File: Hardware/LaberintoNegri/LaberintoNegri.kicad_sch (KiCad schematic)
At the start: 42 parts

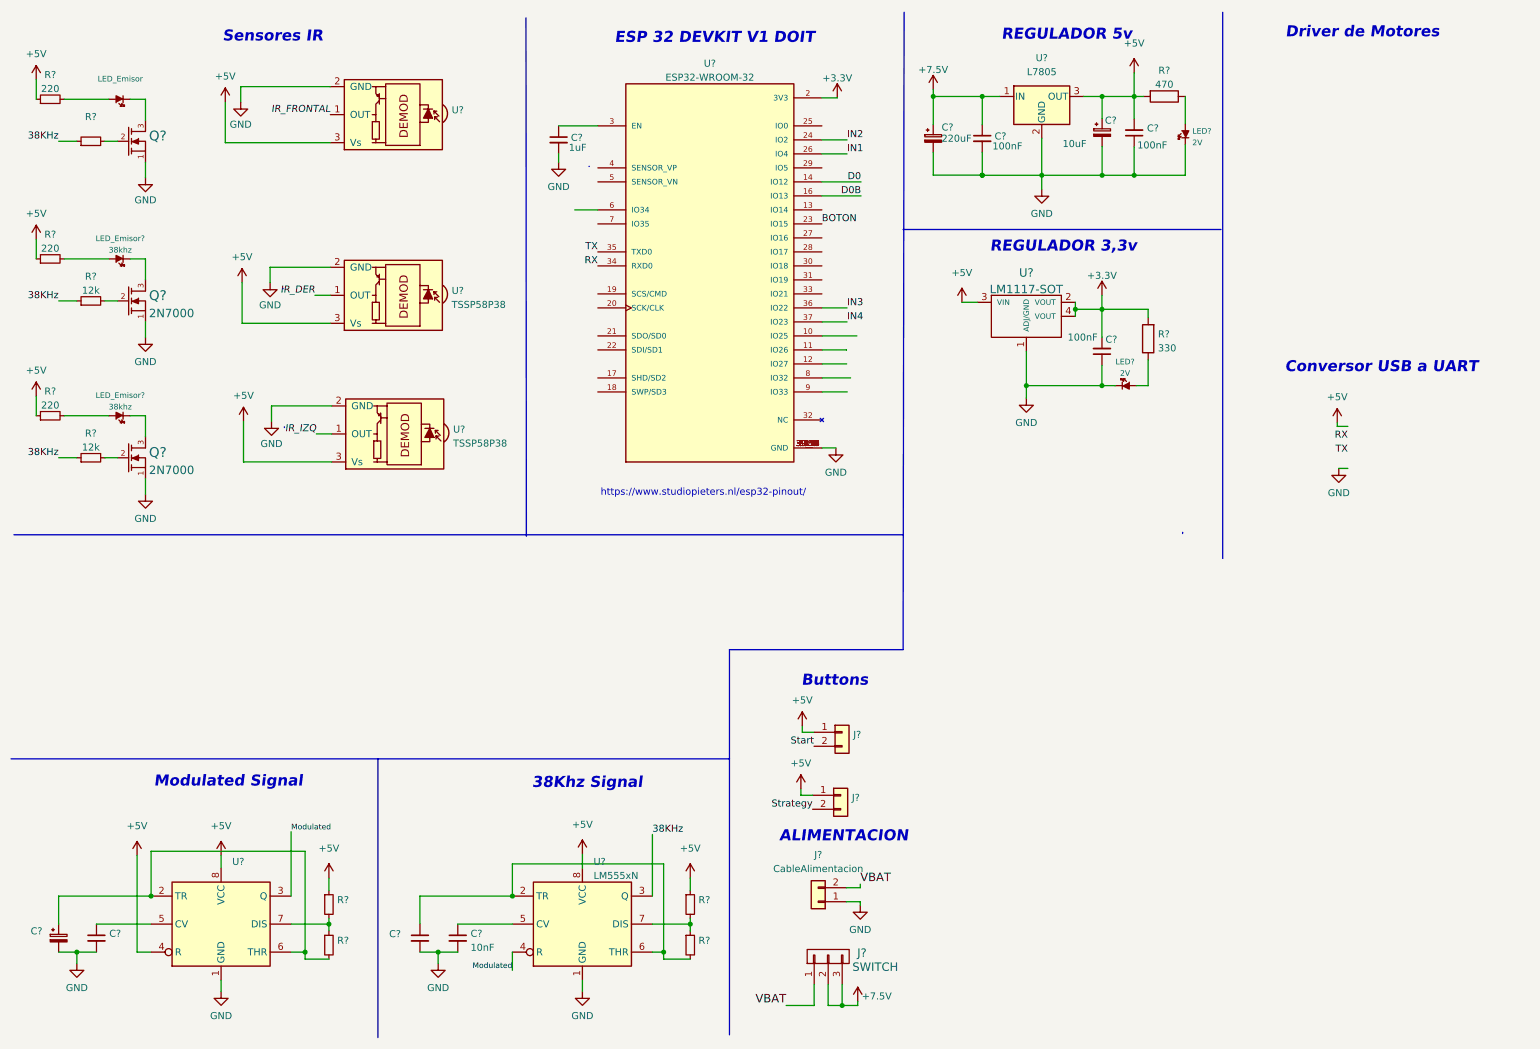
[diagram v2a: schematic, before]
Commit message: subo el sch con el esp32 ya listo como para programar, faltan conexiones y definir el driver
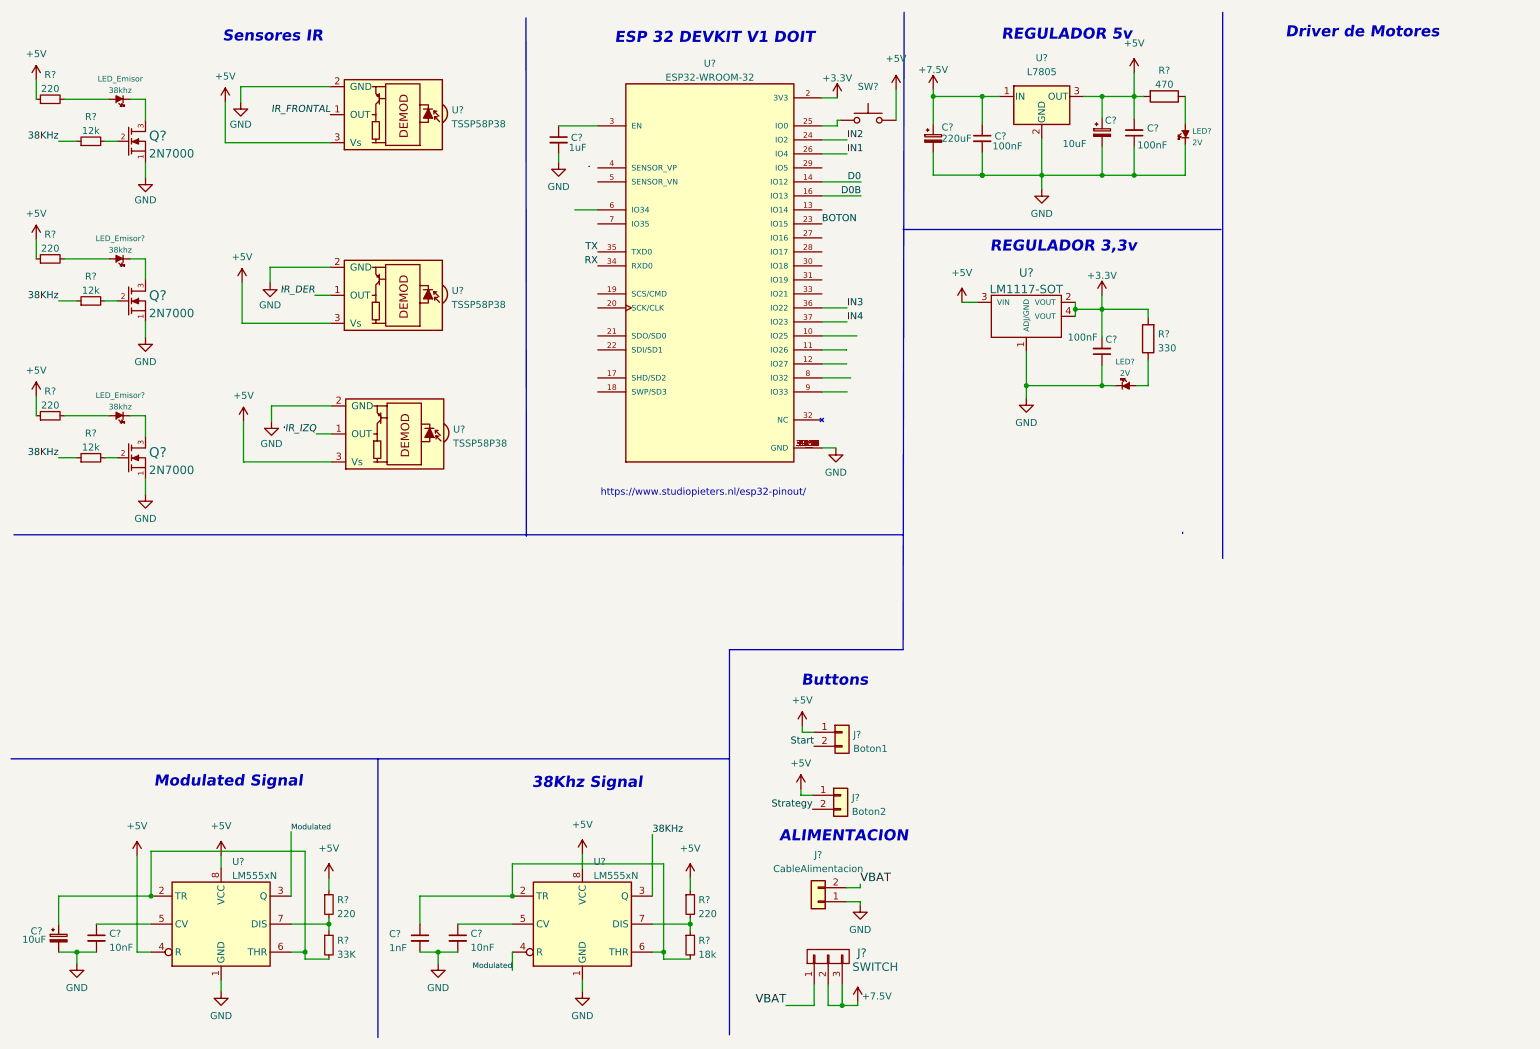
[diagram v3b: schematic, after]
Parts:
- added SW?: SW_Push, symbol EESTN5:SW_Push
- C?: value (none) -> 10uF
- C?: value (none) -> 10nF
- C?: value (none) -> 1nF
- J?: value (none) -> Boton2
- J?: value (none) -> Boton1
- LED_Emisor: value (none) -> 38khz
- Q?: value (none) -> 2N7000; footprint (none) -> EESTN5:SOT23
- R? (x2): value (none) -> 220
- R?: value (none) -> 18k
- R?: value (none) -> 33K
- R?: value (none) -> 12k
- U?: value (none) -> TSSP58P38; footprint (none) -> OptoDevice:Vishay_MINICAST-3Pin
- U?: value (none) -> LM555xN; footprint (none) -> Package_DIP:DIP-8_W7.62mm
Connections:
- net +5V: now also SW?.2
- net at U?.25 (IO0): now also SW?.1
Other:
- note removed: "Conversor USB a UART"
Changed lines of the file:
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@@
     (stroke (width 0) (type default) (color 0 0 0 0))
   )
+  (wire (pts (xy 161.544 32.512) (xy 161.544 31.496))
+    (stroke (width 0) (type default) (color 0 0 0 0))
+  )
   (wire (pts (xy 27.178 177.292) (xy 37.084 177.292))
     (stroke (width 0) (type default) (color 0 0 0 0))
@@
     (stroke (width 0) (type default) (color 0 0 0 0))
   )
+  (wire (pts (xy 161.544 31.496) (xy 162.052 31.496))
+    (stroke (width 0) (type default) (color 0 0 0 0))
+  )
   (wire (pts (xy 65.024 164.084) (xy 37.084 164.084))
     (stroke (width 0) (type default) (color 0 0 0 0))
@@
     (stroke (width 0) (type default) (color 0 0 0 0))
   )
+  (wire (pts (xy 158.75 32.512) (xy 161.544 32.512))
+    (stroke (width 0) (type default) (color 0 0 0 0))
+  )
   (wire (pts (xy 209.55 79.629) (xy 195.834 79.629))
     (stroke (width 0) (type default) (color 0 0 0 0))
@@
     (stroke (width 0) (type default) (color 0 0 0 0))
   )
-  (wire (pts (xy 252.5014 94.6404) (xy 254.1524 94.6404))
-    (stroke (width 0) (type default) (color 0 0 0 0))
-  )
   (wire (pts (xy 28.702 92.71) (xy 30.988 92.71))
     (stroke (width 0) (type default) (color 0 0 0 0))
@@
     (stroke (width 0) (type default) (color 0 0 0 0))
   )
+  (wire (pts (xy 172.212 25.908) (xy 172.212 31.496))
+    (stroke (width 0) (type default) (color 0 0 0 0))
+  )
   (wire (pts (xy 158.75 70.612) (xy 165.1 70.612))
     (stroke (width 0) (type default) (color 0 0 0 0))
@@
     (stroke (width 0) (type default) (color 0 0 0 0))
   )
-  (wire (pts (xy 252.222 87.0204) (xy 252.222 86.36))
-    (stroke (width 0) (type default) (color 0 0 0 0))
-  )
-  (wire (pts (xy 254.1524 87.0204) (xy 252.222 87.0204))
-    (stroke (width 0) (type default) (color 0 0 0 0))
-  )
   (wire (pts (xy 16.256 81.534) (xy 16.256 85.09))
     (stroke (width 0) (type default) (color 0 0 0 0))
@@
     (effects (font (size 2 2) (thickness 0.4) bold italic) (justify left bottom))
   )
-  (text "Conversor USB a UART" (at 242.7224 77.4954 0)
-    (effects (font (size 2 2) (thickness 0.4) bold italic) (justify left bottom))
-  )
   (text "ALIMENTACION\n" (at 151.003 162.5854 0)
     (effects (font (size 2 2) (thickness 0.254) bold italic) (justify left bottom))
@@
     (effects (font (size 1.524 1.524)) (justify right bottom))
   )
-  (label "RX" (at 254.1524 89.5604 180)
-    (effects (font (size 1.27 1.27)) (justify right bottom))
-  )
   (label "IN3" (at 163.322 65.532 0)
     (effects (font (size 1.27 1.27)) (justify left bottom))
@@
     (effects (font (size 1.27 1.27)) (justify left bottom))
   )
-  (label "TX" (at 254.1524 92.1004 180)
-    (effects (font (size 1.27 1.27)) (justify right bottom))
-  )
   (label "D0B" (at 165.862 45.212 180)
     (effects (font (size 1.27 1.27)) (justify right bottom))
@@
       (effects (font (size 1.27 1.27)) (justify left))
     )
-    (property "Value" "" (id 1) (at 13.716 180.086 0)
+    (property "Value" "10uF" (id 1) (at 13.716 180.086 0)
       (effects (font (size 1.27 1.27)) (justify left))
     )
@@
       (effects (font (size 1.27 1.27)) (justify left))
     )
-    (property "Value" "" (id 1) (at 136.3726 175.4382 0)
+    (property "Value" "220" (id 1) (at 136.3726 175.4382 0)
       (effects (font (size 1.27 1.27)) (justify left))
     )
@@
       (effects (font (size 1.27 1.27)) (justify left))
     )
-    (property "Value" "" (id 1) (at 164.1856 156.8962 0)
+    (property "Value" "Boton2" (id 1) (at 164.1856 156.8962 0)
       (effects (font (size 1.27 1.27)) (justify left))
     )
@@
       (effects (font (size 1.016 1.016)))
     )
-    (property "Value" "" (id 1) (at 31.496 26.07 0)
+    (property "Value" "38khz" (id 1) (at 31.496 26.07 0)
       (effects (font (size 1.016 1.016)))
     )
@@
     (pin "7")
   )
-  (symbol (lib_id "power:GND") (at 252.5014 94.6404 0) (unit 1)
-    (in_bom yes) (on_board yes) (fields_autoplaced)
-    (property "Reference" "#PWR?" (id 0) (at 252.5014 100.9904 0)
-      (effects (font (size 1.27 1.27)) hide)
-    )
-    (property "Value" "GND" (id 1) (at 252.5014 99.0838 0))
-    (property "Footprint" "" (id 2) (at 252.5014 94.6404 0)
-      (effects (font (size 1.27 1.27)) hide)
-    )
-    (property "Datasheet" "" (id 3) (at 252.5014 94.6404 0)
-      (effects (font (size 1.27 1.27)) hide)
-    )
-    (pin "1")
-  )
   (symbol (lib_id "power:GND") (at 161.29 90.932 0) (unit 1)
     (in_bom yes) (on_board yes) (fields_autoplaced)
@@
       (effects (font (size 1.27 1.27)) (justify left))
     )
-    (property "Value" "" (id 1) (at 136.3726 182.8042 0)
+    (property "Value" "18k" (id 1) (at 136.3726 182.8042 0)
       (effects (font (size 1.27 1.27)) (justify left))
     )
@@
       (effects (font (size 1.778 1.778)) (justify left))
     )
-    (property "Value" "" (id 1) (at 36.703 37.5515 0)
+    (property "Value" "2N7000" (id 1) (at 36.703 37.5515 0)
       (effects (font (size 1.524 1.524)) (justify left))
     )
-    (property "Footprint" "" (id 2) (at 33.528 35.306 0)
+    (property "Footprint" "EESTN5:SOT23" (id 2) (at 33.528 35.306 0)
       (effects (font (size 1.524 1.524)) hide)
     )
@@
       (effects (font (size 1.27 1.27)) (justify left))
     )
-    (property "Value" "" (id 1) (at 70.8406 175.4382 0)
+    (property "Value" "220" (id 1) (at 70.8406 175.4382 0)
       (effects (font (size 1.27 1.27)) (justify left))
     )
@@
       (effects (font (size 1.27 1.27)) (justify left))
     )
-    (property "Value" "" (id 1) (at 70.8406 182.8042 0)
+    (property "Value" "33K" (id 1) (at 70.8406 182.8042 0)
       (effects (font (size 1.27 1.27)) (justify left))
     )
@@
     (in_bom yes) (on_board yes) (fields_autoplaced)
     (property "Reference" "R?" (id 0) (at 26.162 30.8696 90))
-    (property "Value" "" (id 1) (at 26.162 33.4065 90))
+    (property "Value" "12k" (id 1) (at 26.162 33.4065 90))
     (property "Footprint" "" (id 2) (at 26.162 35.306 0)
       (effects (font (size 1.27 1.27)) hide)
@@
       (effects (font (size 1.27 1.27)) (justify left))
     )
-    (property "Value" "" (id 1) (at 29.5021 181.5405 0)
+    (property "Value" "10nF" (id 1) (at 29.5021 181.5405 0)
       (effects (font (size 1.27 1.27)) (justify left))
     )
@@
     (pin "1")
   )
+  (symbol (lib_id "EESTN5:SW_Push") (at 167.132 31.496 0) (unit 1)
+    (in_bom yes) (on_board yes) (fields_autoplaced)
+    (property "Reference" "SW?" (id 0) (at 167.132 25.4 0))
+    (property "Value" "SW_Push" (id 1) (at 167.132 33.02 0)
+      (effects (font (size 1.27 1.27)) hide)
+    )
+    (property "Footprint" "" (id 2) (at 167.132 26.416 0))
+    (property "Datasheet" "" (id 3) (at 167.132 26.416 0))
+    (pin "1")
+    (pin "2")
+  )
   (symbol (lib_id "power:GND") (at 53.34 28.194 0) (mirror y) (unit 1)
     (in_bom yes) (on_board yes)
@@
       (effects (font (size 1.27 1.27)) (justify right))
     )
-    (property "Value" "" (id 1) (at 91.6078 32.1822 0)
+    (property "Value" "TSSP58P38" (id 1) (at 91.6078 32.1822 0)
       (effects (font (size 1.27 1.27)) (justify right))
     )
-    (property "Footprint" "" (id 2) (at 81.026 20.955 0)
+    (property "Footprint" "OptoDevice:Vishay_MINICAST-3Pin" (id 2) (at 81.026 20.955 0)
       (effects (font (size 1.27 1.27)) hide)
     )
@@
       (effects (font (size 1.27 1.27)) (justify left))
     )
-    (property "Value" "" (id 1) (at 164.4396 145.4662 0)
+    (property "Value" "Boton1" (id 1) (at 164.4396 145.4662 0)
       (effects (font (size 1.27 1.27)) (justify left))
     )
@@
     (pin "2")
   )
-  (symbol (lib_id "power:+5V") (at 252.222 86.36 0) (unit 1)
+  (symbol (lib_id "power:+5V") (at 172.212 25.908 0) (unit 1)
     (in_bom yes) (on_board yes) (fields_autoplaced)
-    (property "Reference" "#PWR?" (id 0) (at 252.222 90.17 0)
+    (property "Reference" "#PWR?" (id 0) (at 172.212 29.718 0)
       (effects (font (size 1.27 1.27)) hide)
     )
-    (property "Value" "+5V" (id 1) (at 252.222 81.6864 0))
-    (property "Footprint" "" (id 2) (at 252.222 86.36 0)
+    (property "Value" "+5V" (id 1) (at 172.212 20.32 0))
+    (property "Footprint" "" (id 2) (at 172.212 25.908 0)
       (effects (font (size 1.27 1.27)) hide)
     )
-    (property "Datasheet" "" (id 3) (at 252.222 86.36 0)
+    (property "Datasheet" "" (id 3) (at 172.212 25.908 0)
       (effects (font (size 1.27 1.27)) hide)
     )
@@
       (effects (font (size 1.27 1.27)) (justify left))
     )
-    (property "Value" "" (id 1) (at 80.264 181.6069 0)
+    (property "Value" "1nF" (id 1) (at 80.264 181.6069 0)
       (effects (font (size 1.27 1.27)) (justify left))
     )
@@
       (effects (font (size 1.27 1.27)) (justify left))
     )
-    (property "Value" "" (id 1) (at 51.8034 168.5091 0)
+    (property "Value" "LM555xN" (id 1) (at 51.8034 168.5091 0)
       (effects (font (size 1.27 1.27)) (justify left))
     )
-    (property "Footprint" "" (id 2) (at 66.294 187.452 0)
+    (property "Footprint" "Package_DIP:DIP-8_W7.62mm" (id 2) (at 66.294 187.452 0)
       (effects (font (size 1.27 1.27)) hide)
     )
@@
       (reference "#PWR?") (unit 1) (value "+5V") (footprint "")
     )
-    (path "/3d87904c-d85c-4bbf-97c6-adb08964aa03"
-      (reference "#PWR?") (unit 1) (value "GND") (footprint "")
-    )
     (path "/4155505f-3687-467b-8149-9afc3d422f5e"
       (reference "#PWR?") (unit 1) (value "GND") (footprint "")
@@
       (reference "#PWR?") (unit 1) (value "+5V") (footprint "")
     )
-    (path "/edf14a6b-0d70-4db0-9e28-784d655ee5be"
+    (path "/ebc5c999-8d10-42a2-b5ba-a39c83e75a6b"
       (reference "#PWR?") (unit 1) (value "+5V") (footprint "")
     )
@@
       (reference "R?") (unit 1) (value "330") (footprint "EESTN5:R_1206")
     )
+    (path "/bc0f5002-fce3-47b4-9c50-95ee45e5b430"
+      (reference "SW?") (unit 1) (value "SW_Push") (footprint "")
+    )
     (path "/3abd8a69-227a-4af4-954d-78af07e50c8d"
